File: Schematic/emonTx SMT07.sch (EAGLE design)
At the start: 113 parts, among them IC1 4066D, IC2 4066D, IC3 LMV324, J1 CON_HEADER_PRG_AVR_ICSP, Q2 DS18B20, U2 ATMEGA32U4, X10 BU-SMA-H, X2 CT2, X3 CT3, X4 STEREOJACK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

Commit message: update schotkey reverse blocking diode pcb footprint to SOD-123
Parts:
- D1: device adafruit:DIODESOD-123 -> adafruit:DIODESOD-323F
- D2: device adafruit:DIODESOD-323F -> adafruit:DIODESOD-123
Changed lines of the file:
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@@
 <?xml version="1.0" encoding="utf-8"?>
 <!DOCTYPE eagle SYSTEM "eagle.dtd">
-<eagle version="6.1">
+<eagle version="6.2">
 <drawing>
 <settings>
@@
 <grid distance="0.1" unitdist="inch" unit="inch" style="lines" multiple="1" display="no" altdistance="0.01" altunitdist="inch" altunit="inch"/>
 <layers>
-<layer number="1" name="Top" color="4" fill="1" visible="no" active="no"/>
-<layer number="2" name="Route2" color="1" fill="3" visible="no" active="no"/>
-<layer number="3" name="Route3" color="4" fill="3" visible="no" active="no"/>
-<layer number="14" name="Route14" color="1" fill="6" visible="no" active="no"/>
-<layer number="15" name="Route15" color="4" fill="6" visible="no" active="no"/>
-<layer number="16" name="Bottom" color="1" fill="1" visible="no" active="no"/>
-<layer number="17" name="Pads" color="2" fill="1" visible="no" active="no"/>
-<layer number="18" name="Vias" color="2" fill="1" visible="no" active="no"/>
-<layer number="19" name="Unrouted" color="6" fill="1" visible="no" active="no"/>
-<layer number="20" name="Dimension" color="15" fill="1" visible="no" active="no"/>
-<layer number="21" name="tPlace" color="7" fill="1" visible="no" active="no"/>
-<layer number="22" name="bPlace" color="7" fill="1" visible="no" active="no"/>
-<layer number="23" name="tOrigins" color="15" fill="1" visible="no" active="no"/>
-<layer number="24" name="bOrigins" color="15" fill="1" visible="no" active="no"/>
-<layer number="25" name="tNames" color="7" fill="1" visible="no" active="no"/>
-<layer number="26" name="bNames" color="7" fill="1" visible="no" active="no"/>
-<layer number="27" name="tValues" color="7" fill="1" visible="no" active="no"/>
-<layer number="28" name="bValues" color="7" fill="1" visible="no" active="no"/>
+<layer number="1" name="Top" color="4" fill="1" visible="yes" active="no"/>
+<layer number="2" name="Route2" color="1" fill="3" visible="yes" active="no"/>
+<layer number="3" name="Route3" color="4" fill="3" visible="yes" active="no"/>
+<layer number="14" name="Route14" color="1" fill="6" visible="yes" active="no"/>
+<layer number="15" name="Route15" color="4" fill="6" visible="yes" active="no"/>
+<layer number="16" name="Bottom" color="1" fill="1" visible="yes" active="no"/>
+<layer number="17" name="Pads" color="2" fill="1" visible="yes" active="no"/>
+<layer number="18" name="Vias" color="2" fill="1" visible="yes" active="no"/>
+<layer number="19" name="Unrouted" color="6" fill="1" visible="yes" active="no"/>
+<layer number="20" name="Dimension" color="15" fill="1" visible="yes" active="no"/>
+<layer number="21" name="tPlace" color="7" fill="1" visible="yes" active="no"/>
+<layer number="22" name="bPlace" color="7" fill="1" visible="yes" active="no"/>
+<layer number="23" name="tOrigins" color="15" fill="1" visible="yes" active="no"/>
+<layer number="24" name="bOrigins" color="15" fill="1" visible="yes" active="no"/>
+<layer number="25" name="tNames" color="7" fill="1" visible="yes" active="no"/>
+<layer number="26" name="bNames" color="7" fill="1" visible="yes" active="no"/>
+<layer number="27" name="tValues" color="7" fill="1" visible="yes" active="no"/>
+<layer number="28" name="bValues" color="7" fill="1" visible="yes" active="no"/>
 <layer number="29" name="tStop" color="7" fill="3" visible="no" active="no"/>
 <layer number="30" name="bStop" color="7" fill="6" visible="no" active="no"/>
@@
 <layer number="35" name="tGlue" color="7" fill="4" visible="no" active="no"/>
 <layer number="36" name="bGlue" color="7" fill="5" visible="no" active="no"/>
-<layer number="37" name="tTest" color="7" fill="1" visible="no" active="no"/>
-<layer number="38" name="bTest" color="7" fill="1" visible="no" active="no"/>
+<layer number="37" name="tTest" color="7" fill="1" visible="yes" active="no"/>
+<layer number="38" name="bTest" color="7" fill="1" visible="yes" active="no"/>
 <layer number="39" name="tKeepout" color="4" fill="11" visible="no" active="no"/>
 <layer number="40" name="bKeepout" color="1" fill="11" visible="no" active="no"/>
@@
 <layer number="44" name="Drills" color="7" fill="1" visible="no" active="no"/>
 <layer number="45" name="Holes" color="7" fill="1" visible="no" active="no"/>
-<layer number="46" name="Milling" color="3" fill="1" visible="no" active="no"/>
-<layer number="47" name="Measures" color="7" fill="1" visible="no" active="no"/>
-<layer number="48" name="Document" color="7" fill="1" visible="no" active="no"/>
-<layer number="49" name="Reference" color="7" fill="1" visible="no" active="no"/>
-<layer number="50" name="dxf" color="7" fill="1" visible="no" active="no"/>
-<layer number="51" name="tDocu" color="7" fill="1" visible="no" active="no"/>
-<layer number="52" name="bDocu" color="7" fill="1" visible="no" active="no"/>
-<layer number="53" name="tGND_GNDA" color="7" fill="9" visible="no" active="no"/>
-<layer number="54" name="bGND_GNDA" color="1" fill="9" visible="no" active="no"/>
-<layer number="56" name="wert" color="7" fill="1" visible="no" active="no"/>
+<layer number="46" name="Milling" color="3" fill="1" visible="yes" active="no"/>
+<layer number="47" name="Measures" color="7" fill="1" visible="yes" active="no"/>
+<layer number="48" name="Document" color="7" fill="1" visible="yes" active="no"/>
+<layer number="49" name="Reference" color="7" fill="1" visible="yes" active="no"/>
+<layer number="50" name="dxf" color="7" fill="1" visible="yes" active="no"/>
+<layer number="51" name="tDocu" color="7" fill="1" visible="yes" active="no"/>
+<layer number="52" name="bDocu" color="7" fill="1" visible="yes" active="no"/>
+<layer number="53" name="tGND_GNDA" color="7" fill="9" visible="yes" active="no"/>
+<layer number="54" name="bGND_GNDA" color="1" fill="9" visible="yes" active="no"/>
+<layer number="56" name="wert" color="7" fill="1" visible="yes" active="no"/>
 <layer number="91" name="Nets" color="2" fill="1" visible="yes" active="yes"/>
 <layer number="92" name="Busses" color="1" fill="1" visible="yes" active="yes"/>
@@
 <part name="P+3" library="supply1" deviceset="+5V" device=""/>
 <part name="P+5" library="supply1" deviceset="+5V" device=""/>
-<part name="D2" library="adafruit" deviceset="DIODE" device="SOD-323F" value="0.5A schottky"/>
+<part name="D2" library="adafruit" deviceset="DIODE" device="SOD-123" value="0.5A schottky"/>
 <part name="3XAAA" library="Battery Holders" deviceset="3X_AAA_BATTERY_HOLDER" device="" value="4.5V"/>
 <part name="X10" library="con-coax" deviceset="BU-SMA-H" device=""/>
@@
 <part name="F1" library="rcl" deviceset="R-EU_" device="R1210" value="500mA"/>
 <part name="U$6" library="adafruit" deviceset="XBEE" device=""/>
-<part name="D1" library="adafruit" deviceset="DIODE" device="SOD-123" value="1N4148 30V 150mA (Av)"/>
+<part name="D1" library="adafruit" deviceset="DIODE" device="SOD-323F" value="1N4148 30V 150mA (Av)"/>
 <part name="AGND5" library="supply1" deviceset="AGND" device=""/>
 <part name="U$9" library="SparkFun" deviceset="RF-LINK_TX" device="" value="ASK RF Tx"/>

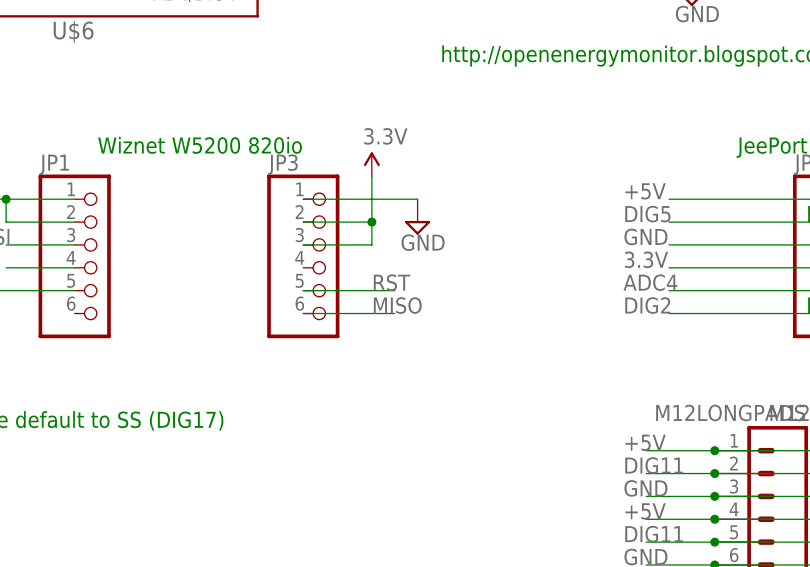
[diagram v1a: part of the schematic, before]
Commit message: connect wiznet reset to dig5, need to route
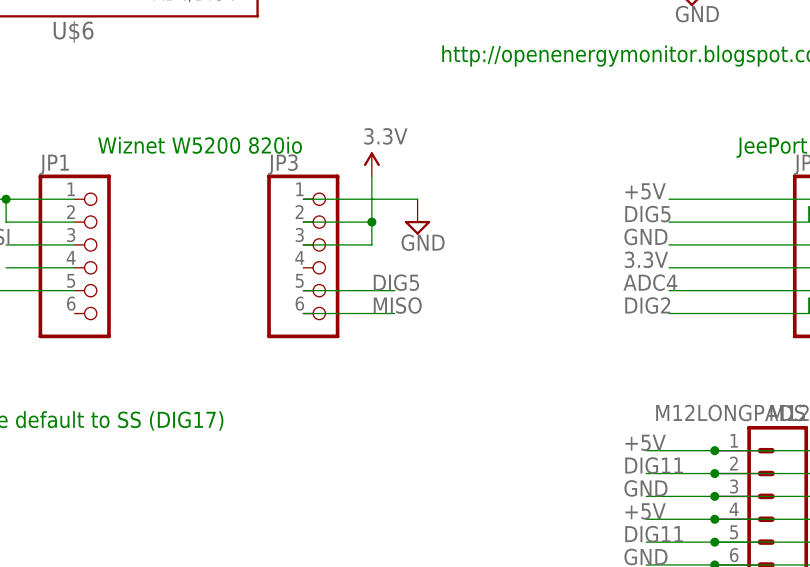
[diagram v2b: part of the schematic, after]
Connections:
- net DIG5: now also JP3.5
- net RST: no longer JP3.5
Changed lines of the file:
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@@
 <grid distance="0.1" unitdist="inch" unit="inch" style="lines" multiple="1" display="no" altdistance="0.01" altunitdist="inch" altunit="inch"/>
 <layers>
-<layer number="1" name="Top" color="4" fill="1" visible="yes" active="no"/>
-<layer number="2" name="Route2" color="1" fill="3" visible="yes" active="no"/>
-<layer number="3" name="Route3" color="4" fill="3" visible="yes" active="no"/>
-<layer number="14" name="Route14" color="1" fill="6" visible="yes" active="no"/>
-<layer number="15" name="Route15" color="4" fill="6" visible="yes" active="no"/>
-<layer number="16" name="Bottom" color="1" fill="1" visible="yes" active="no"/>
-<layer number="17" name="Pads" color="2" fill="1" visible="yes" active="no"/>
-<layer number="18" name="Vias" color="2" fill="1" visible="yes" active="no"/>
-<layer number="19" name="Unrouted" color="6" fill="1" visible="yes" active="no"/>
-<layer number="20" name="Dimension" color="15" fill="1" visible="yes" active="no"/>
-<layer number="21" name="tPlace" color="7" fill="1" visible="yes" active="no"/>
-<layer number="22" name="bPlace" color="7" fill="1" visible="yes" active="no"/>
-<layer number="23" name="tOrigins" color="15" fill="1" visible="yes" active="no"/>
-<layer number="24" name="bOrigins" color="15" fill="1" visible="yes" active="no"/>
-<layer number="25" name="tNames" color="7" fill="1" visible="yes" active="no"/>
-<layer number="26" name="bNames" color="7" fill="1" visible="yes" active="no"/>
-<layer number="27" name="tValues" color="7" fill="1" visible="yes" active="no"/>
-<layer number="28" name="bValues" color="7" fill="1" visible="yes" active="no"/>
+<layer number="1" name="Top" color="4" fill="1" visible="no" active="no"/>
+<layer number="2" name="Route2" color="1" fill="3" visible="no" active="no"/>
+<layer number="3" name="Route3" color="4" fill="3" visible="no" active="no"/>
+<layer number="14" name="Route14" color="1" fill="6" visible="no" active="no"/>
+<layer number="15" name="Route15" color="4" fill="6" visible="no" active="no"/>
+<layer number="16" name="Bottom" color="1" fill="1" visible="no" active="no"/>
+<layer number="17" name="Pads" color="2" fill="1" visible="no" active="no"/>
+<layer number="18" name="Vias" color="2" fill="1" visible="no" active="no"/>
+<layer number="19" name="Unrouted" color="6" fill="1" visible="no" active="no"/>
+<layer number="20" name="Dimension" color="15" fill="1" visible="no" active="no"/>
+<layer number="21" name="tPlace" color="7" fill="1" visible="no" active="no"/>
+<layer number="22" name="bPlace" color="7" fill="1" visible="no" active="no"/>
+<layer number="23" name="tOrigins" color="15" fill="1" visible="no" active="no"/>
+<layer number="24" name="bOrigins" color="15" fill="1" visible="no" active="no"/>
+<layer number="25" name="tNames" color="7" fill="1" visible="no" active="no"/>
+<layer number="26" name="bNames" color="7" fill="1" visible="no" active="no"/>
+<layer number="27" name="tValues" color="7" fill="1" visible="no" active="no"/>
+<layer number="28" name="bValues" color="7" fill="1" visible="no" active="no"/>
 <layer number="29" name="tStop" color="7" fill="3" visible="no" active="no"/>
 <layer number="30" name="bStop" color="7" fill="6" visible="no" active="no"/>
@@
 <layer number="35" name="tGlue" color="7" fill="4" visible="no" active="no"/>
 <layer number="36" name="bGlue" color="7" fill="5" visible="no" active="no"/>
-<layer number="37" name="tTest" color="7" fill="1" visible="yes" active="no"/>
-<layer number="38" name="bTest" color="7" fill="1" visible="yes" active="no"/>
+<layer number="37" name="tTest" color="7" fill="1" visible="no" active="no"/>
+<layer number="38" name="bTest" color="7" fill="1" visible="no" active="no"/>
 <layer number="39" name="tKeepout" color="4" fill="11" visible="no" active="no"/>
 <layer number="40" name="bKeepout" color="1" fill="11" visible="no" active="no"/>
@@
 <layer number="44" name="Drills" color="7" fill="1" visible="no" active="no"/>
 <layer number="45" name="Holes" color="7" fill="1" visible="no" active="no"/>
-<layer number="46" name="Milling" color="3" fill="1" visible="yes" active="no"/>
-<layer number="47" name="Measures" color="7" fill="1" visible="yes" active="no"/>
-<layer number="48" name="Document" color="7" fill="1" visible="yes" active="no"/>
-<layer number="49" name="Reference" color="7" fill="1" visible="yes" active="no"/>
-<layer number="50" name="dxf" color="7" fill="1" visible="yes" active="no"/>
-<layer number="51" name="tDocu" color="7" fill="1" visible="yes" active="no"/>
-<layer number="52" name="bDocu" color="7" fill="1" visible="yes" active="no"/>
-<layer number="53" name="tGND_GNDA" color="7" fill="9" visible="yes" active="no"/>
-<layer number="54" name="bGND_GNDA" color="1" fill="9" visible="yes" active="no"/>
-<layer number="56" name="wert" color="7" fill="1" visible="yes" active="no"/>
+<layer number="46" name="Milling" color="3" fill="1" visible="no" active="no"/>
+<layer number="47" name="Measures" color="7" fill="1" visible="no" active="no"/>
+<layer number="48" name="Document" color="7" fill="1" visible="no" active="no"/>
+<layer number="49" name="Reference" color="7" fill="1" visible="no" active="no"/>
+<layer number="50" name="dxf" color="7" fill="1" visible="no" active="no"/>
+<layer number="51" name="tDocu" color="7" fill="1" visible="no" active="no"/>
+<layer number="52" name="bDocu" color="7" fill="1" visible="no" active="no"/>
+<layer number="53" name="tGND_GNDA" color="7" fill="9" visible="no" active="no"/>
+<layer number="54" name="bGND_GNDA" color="1" fill="9" visible="no" active="no"/>
+<layer number="56" name="wert" color="7" fill="1" visible="no" active="no"/>
 <layer number="91" name="Nets" color="2" fill="1" visible="yes" active="yes"/>
 <layer number="92" name="Busses" color="1" fill="1" visible="yes" active="yes"/>
@@
 <junction x="12.7" y="154.94"/>
 </segment>
-<segment>
-<pinref part="JP3" gate="A" pin="5"/>
-<wire x1="314.96" y1="132.08" x2="325.12" y2="132.08" width="0.1524" layer="91"/>
-<label x="322.58" y="132.08" size="1.778" layer="95"/>
-</segment>
 </net>
 <net name="N$20" class="0">
@@
 <wire x1="355.6" y1="139.7" x2="373.38" y2="139.7" width="0.1524" layer="91"/>
 </segment>
-</net>
+<segment>
+<pinref part="JP3" gate="A" pin="5"/>
+<wire x1="314.96" y1="132.08" x2="325.12" y2="132.08" width="0.1524" layer="91"/>
+<label x="322.58" y="132.08" size="1.778" layer="95"/>
+</segment>
+</net>
